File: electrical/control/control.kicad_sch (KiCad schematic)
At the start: 46 parts, among them J1 USB4105-GF-A, J3 SWD, J4 QWIIC, J5 TC2030-NL, J6 UART, SW1 BOOT, U1 RP2040, U2 ABPMRRV001PD2A3, U4 W25Q16JVSSIQ, U5 LP5907MFX-3.3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

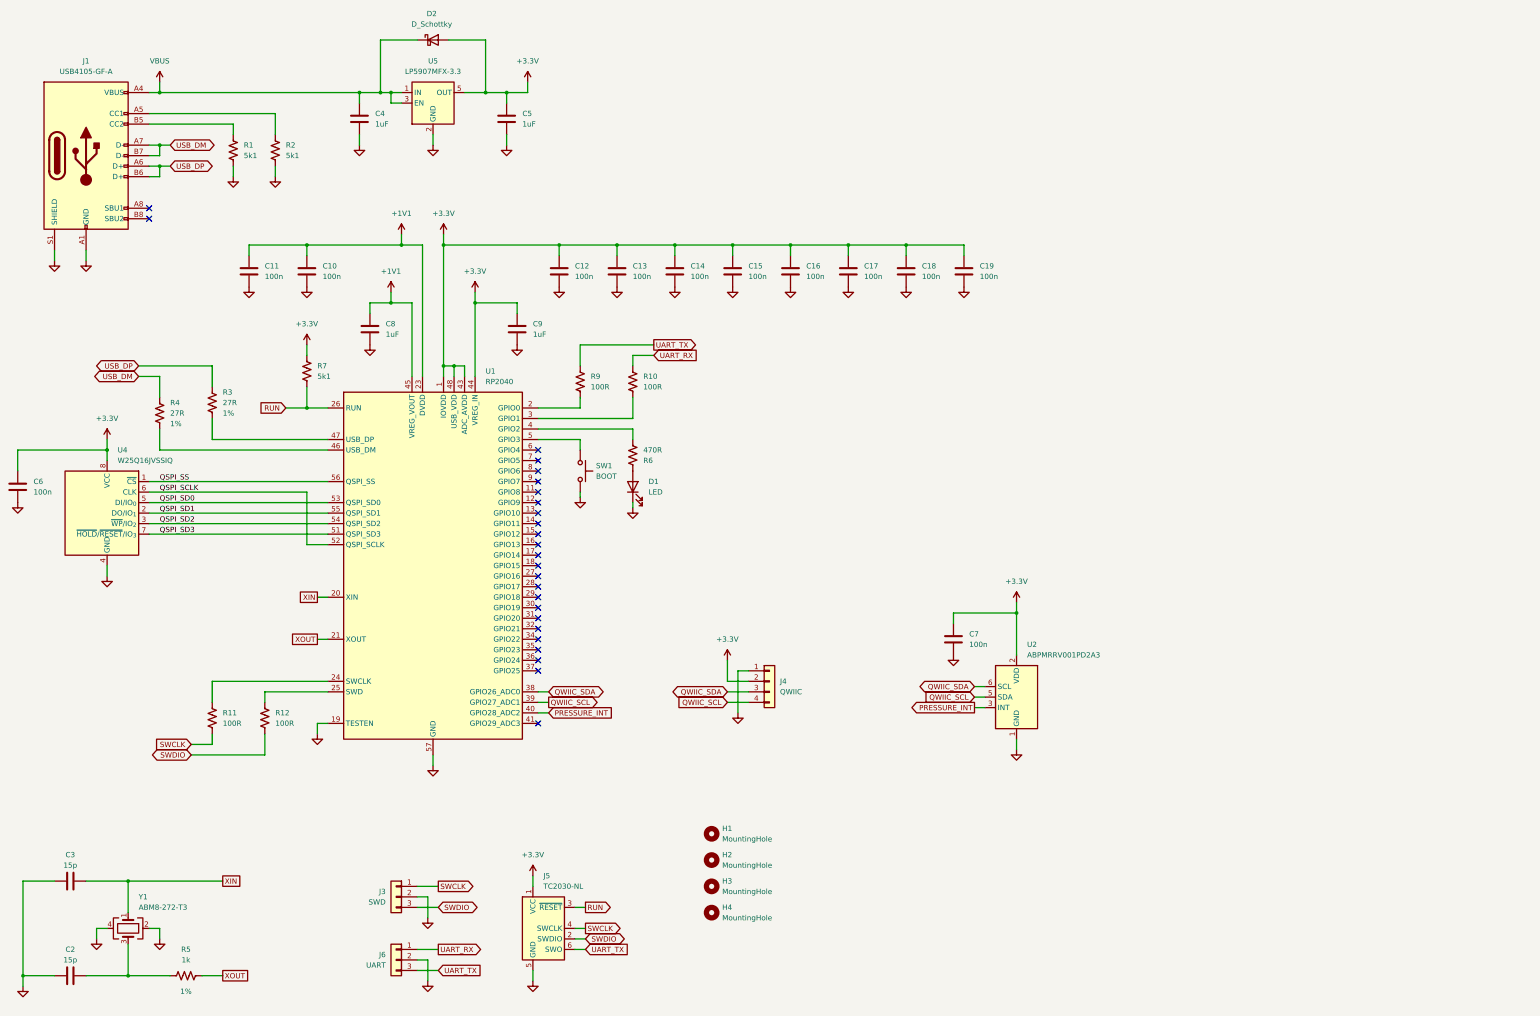
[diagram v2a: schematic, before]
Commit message: Clean up control board schematic
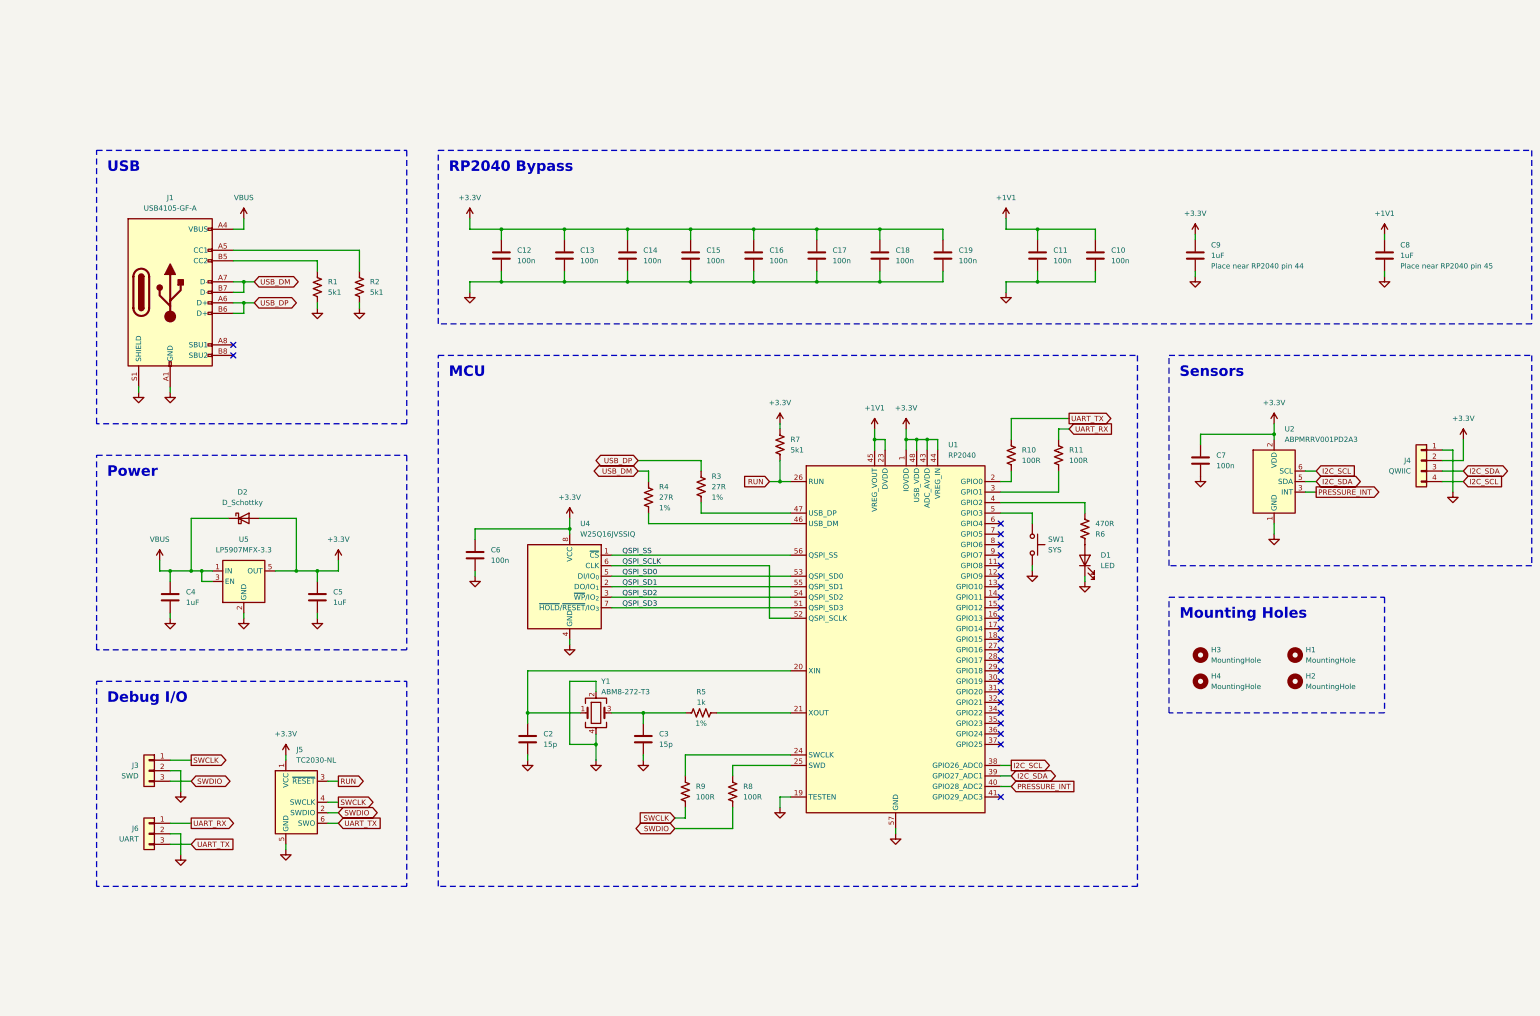
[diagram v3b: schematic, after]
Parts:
- removed R12: 100R, Resistor_SMD:R_0402_1005Metric, symbol Device:R_US
- added R8: 100R, Resistor_SMD:R_0402_1005Metric, symbol Device:R_US
- C8: Note (none) -> Place near RP2040 pin 45
- C9: Note (none) -> Place near RP2040 pin 44
- SW1: value BOOT -> SYS
- U4: LCSC (none) -> C131025
- Y1: footprint (none) -> Crystal:Crystal_SMD_3225-4Pin_3.2x2.5mm; LCSC (none) -> C20625731
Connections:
- net GND: now also C2.2, C3.2; no longer C2.1, C3.1
- net SWCLK: now also R9.2; no longer R11.1
- net SWDIO: now also R8.2
- net UART_RX: now also R11.1; no longer R10.2
- net UART_TX: now also R10.1; no longer R9.2
- net at R5.1, Y1.3: now also C3.1; no longer C2.2
- net at R11.2: now also U1.3 (GPIO1); no longer U1.24 (SWCLK)
- net at U1.2 (GPIO0): now also R10.2; no longer R9.1
- net at U1.25 (SWD): now also R8.1
- net QWIIC_SCL renamed I2C_SDA
- net I2C_SDA: now also J4.3 (Pin_3); no longer J4.4 (Pin_4)
- net QWIIC_SDA renamed I2C_SCL
- net I2C_SCL: now also J4.4 (Pin_4); no longer J4.3 (Pin_3)
- net XIN: no longer names the net of U1.20 (XIN), Y1.1
- net XIN: now also C2.1; no longer C3.2
- net XOUT: no longer names the net of R5.2, U1.21 (XOUT)
- new net: R9.1, U1.24 (SWCLK)
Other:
- note added: "Debug I/O"
- note added: "MCU"
- note added: "Mounting Holes"
- note added: "Power"
- note added: "RP2040 Bypass"
- note added: "Sensors"
- note added: "USB"
- moved on the sheet: C10, C11, C12, C13, C14, C15, C16, C17, C18, C19, C4, C5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

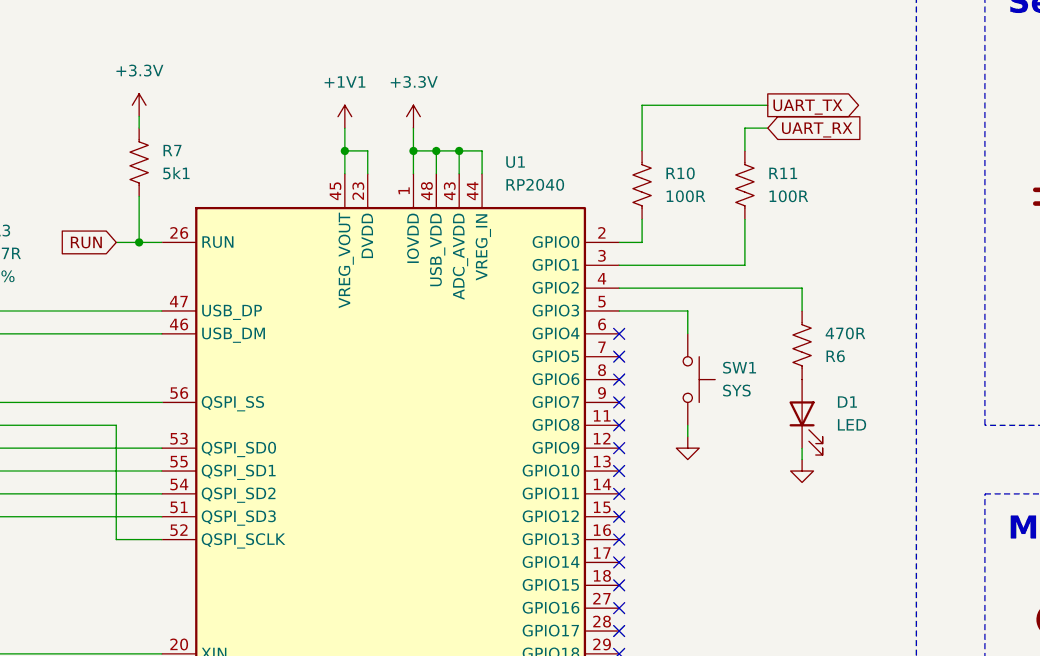
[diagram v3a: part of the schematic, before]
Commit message: Adjust LED and resistor selection
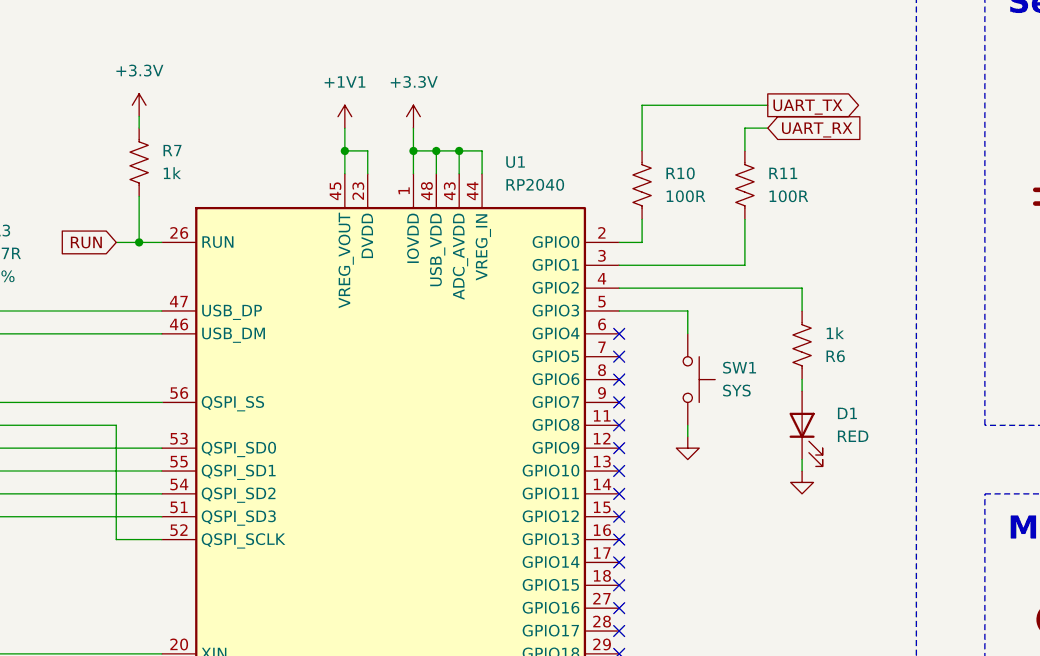
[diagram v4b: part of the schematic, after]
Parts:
- D1: value LED -> RED; LCSC (none) -> C2286
- R6: value 470R -> 1k
- R7: value 5k1 -> 1k
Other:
- moved on the sheet: D1
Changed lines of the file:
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@@
 	(wire
 		(pts
+			(xy 280.67 147.32) (xy 280.67 146.05)
+		)
+		(stroke
+			(width 0)
+			(type default)
+		)
+	)
+	(wire
+		(pts
 			(xy 353.06 71.12) (xy 353.06 72.39)
 		)
@@
 	(wire
 		(pts
-			(xy 280.67 154.94) (xy 280.67 153.67)
+			(xy 280.67 156.21) (xy 280.67 154.94)
 		)
 		(stroke
@@
 	(symbol
 		(lib_id "Device:LED")
-		(at 280.67 149.86 90)
+		(at 280.67 151.13 90)
 		(unit 1)
 		(exclude_from_sim no)
@@
 		(dnp no)
 		(property "Reference" "D1"
-			(at 284.48 148.59 90)
+			(at 284.48 149.86 90)
 			(effects
 				(font
@@
 			)
 		)
-		(property "Value" "LED"
-			(at 284.48 151.13 90)
+		(property "Value" "RED"
+			(at 284.48 152.4 90)
 			(effects
 				(font
@@
 		)
 		(property "Footprint" "LED_SMD:LED_0603_1608Metric"
-			(at 280.67 149.86 0)
+			(at 280.67 151.13 0)
 			(effects
 				(font
@@
 		)
 		(property "Datasheet" "~"
-			(at 280.67 149.86 0)
+			(at 280.67 151.13 0)
 			(effects
 				(font
@@
 		)
 		(property "Description" "Light emitting diode"
-			(at 280.67 149.86 0)
+			(at 280.67 151.13 0)
 			(effects
 				(font
@@
 		)
 		(property "Sim.Pins" "1=K 2=A"
-			(at 280.67 149.86 0)
+			(at 280.67 151.13 0)
+			(effects
+				(font
+					(size 1.27 1.27)
+				)
+				(hide yes)
+			)
+		)
+		(property "LCSC" "C2286"
+			(at 280.67 151.13 90)
 			(effects
 				(font
@@
 			)
 		)
-		(property "Value" "5k1"
+		(property "Value" "1k"
 			(at 209.55 123.1899 0)
 			(effects
@@
 	(symbol
 		(lib_id "power:GND")
-		(at 280.67 154.94 0)
+		(at 280.67 156.21 0)
 		(unit 1)
 		(exclude_from_sim no)
@@
 		(fields_autoplaced yes)
 		(property "Reference" "#PWR024"
-			(at 280.67 161.29 0)
+			(at 280.67 162.56 0)
 			(effects
 				(font
@@
 		)
 		(property "Value" "GND"
-			(at 280.67 160.02 0)
+			(at 280.67 161.29 0)
 			(effects
 				(font
@@
 		)
 		(property "Footprint" ""
-			(at 280.67 154.94 0)
+			(at 280.67 156.21 0)
 			(effects
 				(font
@@
 		)
 		(property "Datasheet" ""
-			(at 280.67 154.94 0)
+			(at 280.67 156.21 0)
 			(effects
 				(font
@@
 		)
 		(property "Description" "Power symbol creates a global label with name \"GND\" , ground"
-			(at 280.67 154.94 0)
+			(at 280.67 156.21 0)
 			(effects
 				(font
@@
 			)
 		)
-		(property "Value" "470R"
+		(property "Value" "1k"
 			(at 283.21 140.97 0)
 			(effects

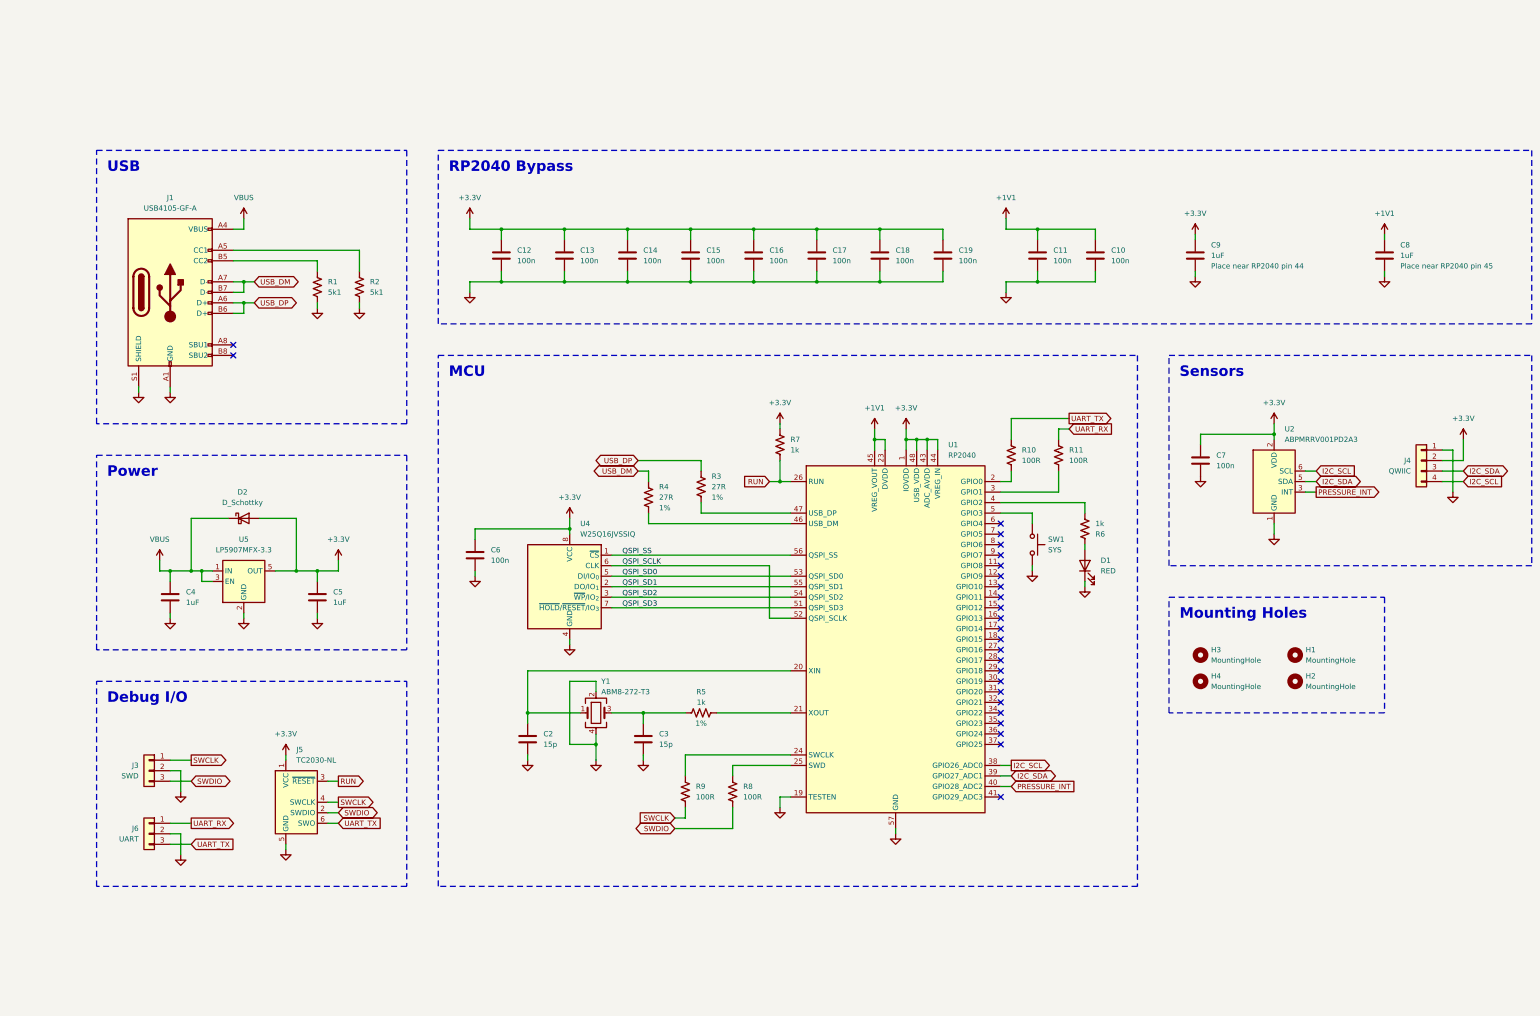
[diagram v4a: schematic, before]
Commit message: Set JLC part numbers for various components
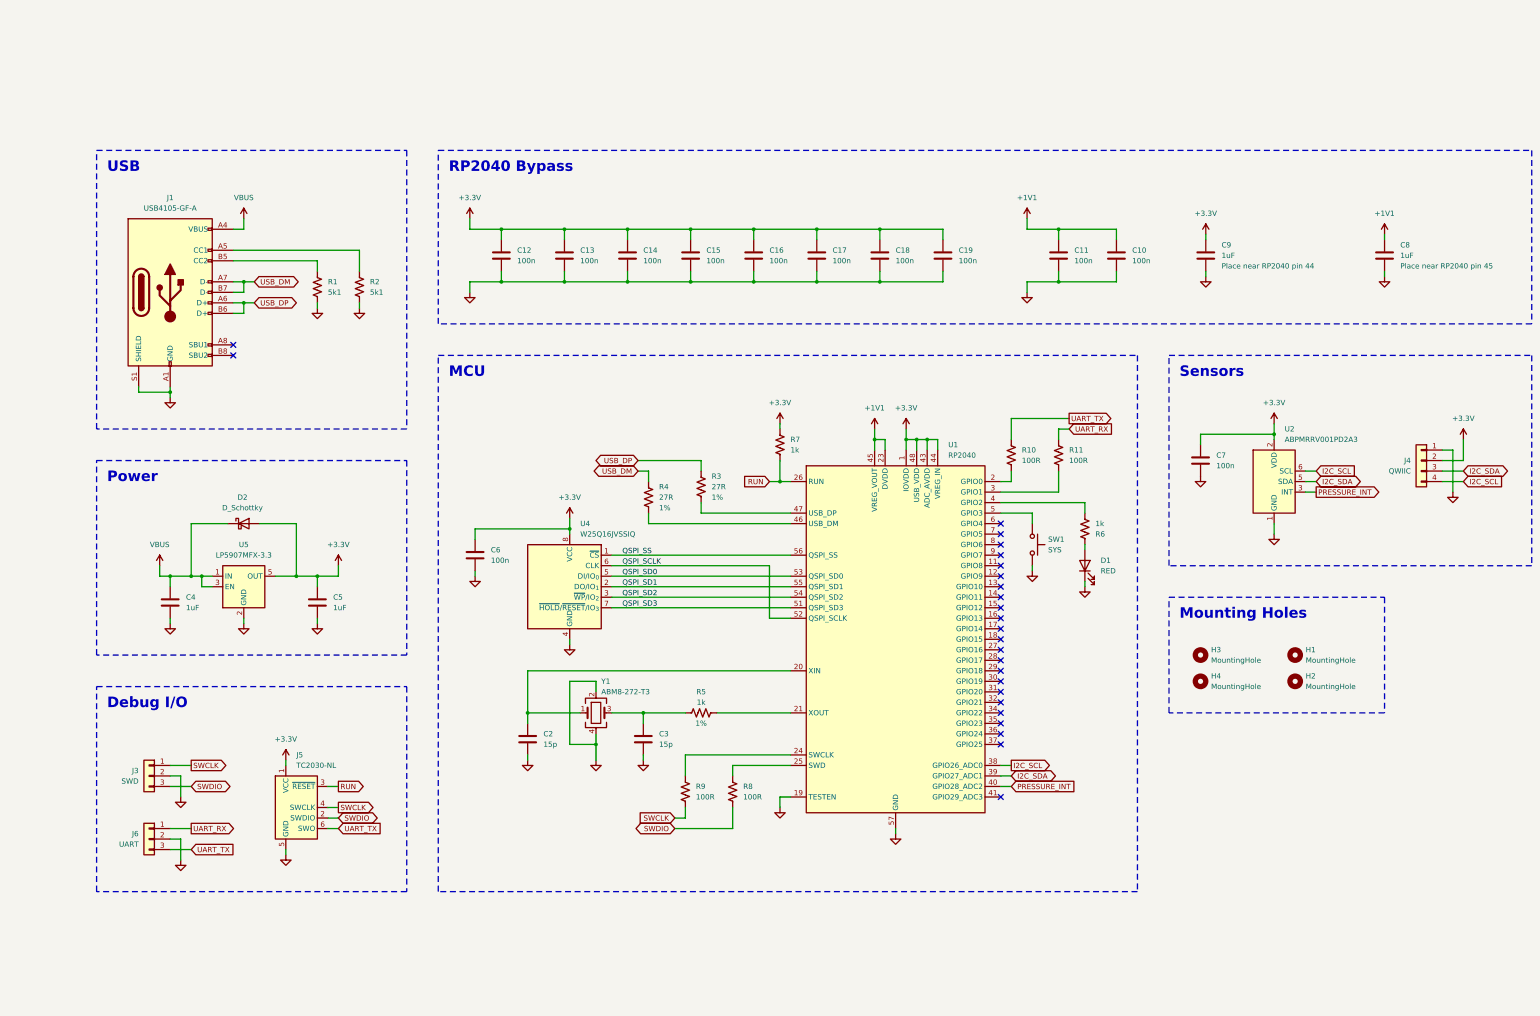
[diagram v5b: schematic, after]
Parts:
- C10, C11, C12, C13, C14, C15, C16, C17, C18, C19, C6, C7: LCSC (none) -> C1525
- C2, C3: LCSC (none) -> C1548
- C4, C5, C8, C9: LCSC (none) -> C52923
- D2: LCSC (none) -> C5261070
- J3, J6: LCSC (none) -> C160403
- J4: LCSC (none) -> C160404
- R1, R2: LCSC (none) -> C25905
- R10, R11, R8, R9: LCSC (none) -> C25076
- R5, R6, R7: LCSC (none) -> C11702
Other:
- moved on the sheet: C10, C11, C4, C5, C9, D2, J3, J5, J6, U5
